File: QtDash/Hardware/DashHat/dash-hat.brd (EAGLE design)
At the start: 120.9 x 74.9 mm, 179 parts, among them IC1 LMV614, IC10 MAX9924, IC11 ZXTR2105FQ, IC12 SN65HVD230D, IC13 MCP2515, IC2 MCP3X083008, IC3 MCP23017SS, IC4 LM358D, IC5 IL300, IC6 TSV912D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

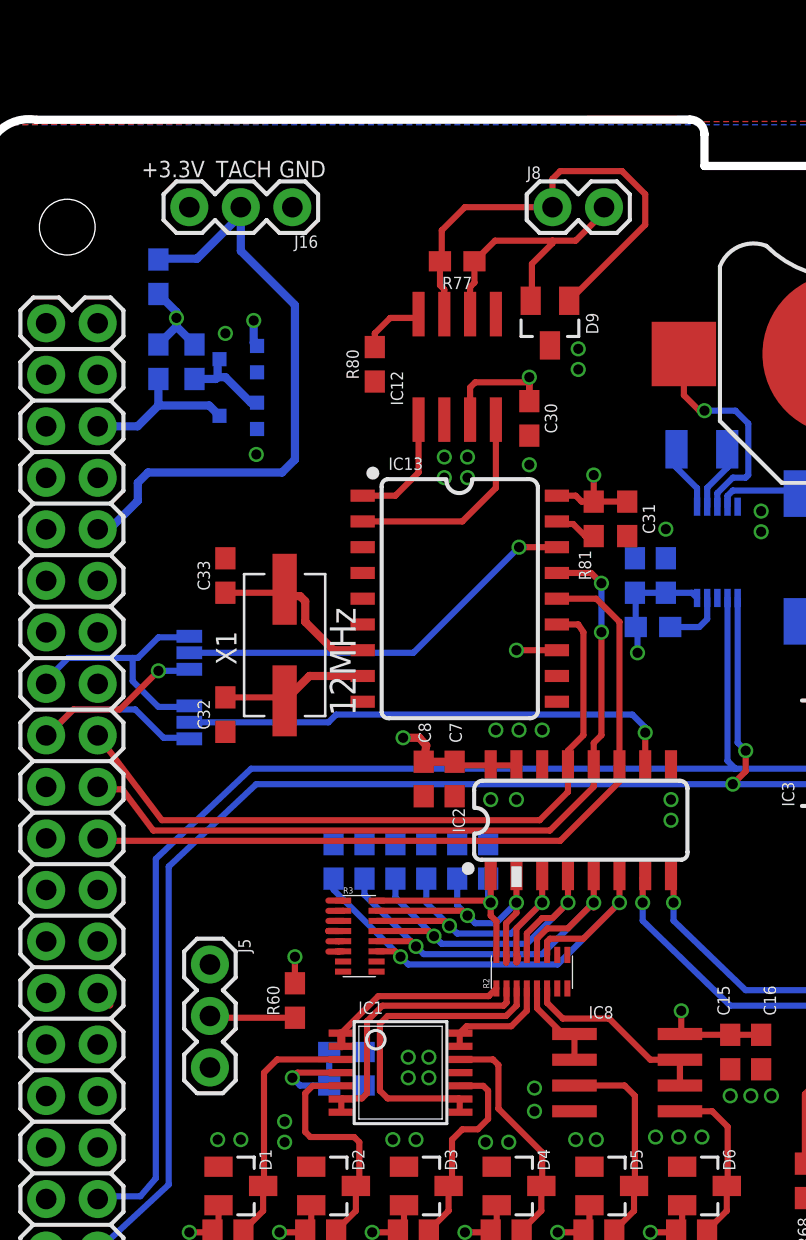
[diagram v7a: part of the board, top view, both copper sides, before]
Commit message: topic/hardware-revc: 	- gerbers generated for rev c 	- pcb's ordered from JLC pcb 	- rev c board preview images generated
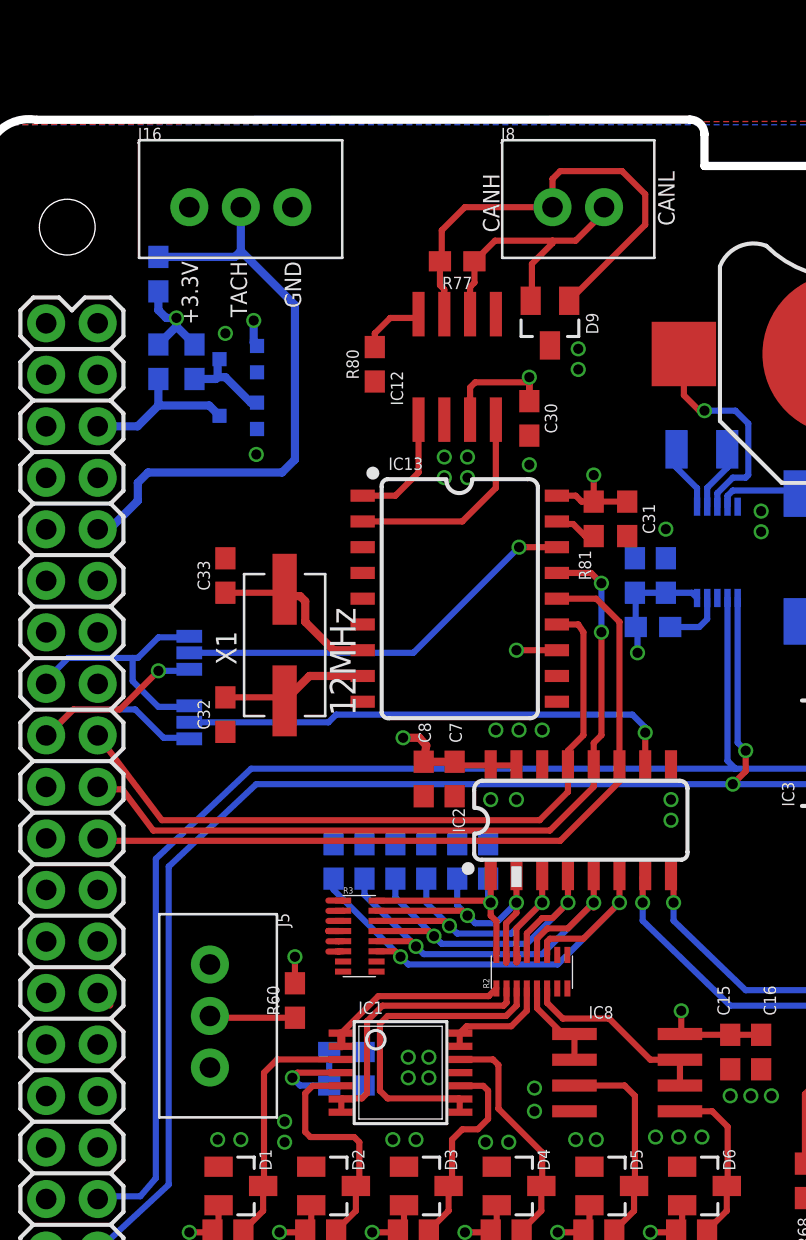
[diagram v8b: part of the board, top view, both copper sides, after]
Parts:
- J16, J5: device SparkFun-Connectors:1X03 -> digital_dash:1X03_JST-XHP
- J8: device digital_dash:1X02 -> digital_dash:1X02_JST-XHP
- moved J16 5.08 mm to (10.2, 62.5), turned to 0 degrees
- moved R76 0.13 mm to (8.64, 59.2)
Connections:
- net 3.3V: now also J16.1; no longer J16.3
- net GND: now also J16.3; no longer J16.1
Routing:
- net GPIO6: track 30.6 -> 29.8 mm
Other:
- board text added: "CANH"
- board text added: "CANL"
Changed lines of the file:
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@@
 Rev C. May 2022
 @whitfijs</text>
-<text x="10.922" y="64.77" size="0.8128" layer="21" font="vector" rot="R180">+3.3V</text>
-<text x="16.891" y="64.77" size="0.8128" layer="21" font="vector" rot="R180">GND</text>
-<text x="14.224" y="64.77" size="0.8128" layer="21" font="vector" rot="R180">TACH</text>
+<text x="9.779" y="59.817" size="0.8128" layer="21" font="vector" rot="R270">+3.3V</text>
+<text x="14.859" y="59.817" size="0.8128" layer="21" font="vector" rot="R270">GND</text>
+<text x="12.192" y="59.817" size="0.8128" layer="21" font="vector" rot="R270">TACH</text>
 <circle x="4.7878" y="18.439" radius="1" width="0.001" layer="57"/>
 <circle x="4.6578" y="27.779" radius="1" width="0.001" layer="57"/>
@@
 <text x="72.39" y="61.595" size="1.016" layer="25" font="vector">12V Switched</text>
 <text x="72.39" y="64.135" size="1.016" layer="25" font="vector">GND</text>
+<text x="33.274" y="64.262" size="0.8128" layer="21" font="vector" rot="R270">CANL</text>
+<text x="24.638" y="64.135" size="0.8128" layer="21" font="vector" rot="R270">CANH</text>
 </plain>
 <attributes>
@@
 <attribute name="SF_SKU" value="COM-08229" x="40.259" y="45.212" size="1.778" layer="28" rot="MR90" display="off"/>
 </element>
-<element name="J16" library="SparkFun-Connectors" package="1X03" value="TACH_IN" x="15.24" y="62.484" rot="R180">
-<attribute name="PROD_ID" value="XXX-00000" x="15.24" y="62.484" size="1.778" layer="27" rot="R180" display="off"/>
-</element>
-<element name="R76" library="digital_dash" package="0603" value="20k" x="8.636" y="59.055" rot="MR270"/>
+<element name="J16" library="digital_dash" package="1X03_JST-XHP" value="TACH_IN" x="10.16" y="62.484"/>
+<element name="R76" library="digital_dash" package="0603" value="20k" x="8.636" y="59.182" rot="MR270"/>
 <element name="R82" library="digital_dash" package="0617/17" value="RES_D+" x="109.474" y="47.879" smashed="yes" rot="R90">
 <attribute name="NAME" x="112.9284" y="56.261" size="1.27" layer="25" font="vector" ratio="10" rot="R270"/>
@@
 <element name="J3" library="digital_dash" package="MOLEX-1053141204" value="CONN_04RIGHT-ANGLE" x="69.469" y="63.373"/>
 <element name="J4" library="digital_dash" package="MOLEX-1053101104" value="CONN_04" x="43.688" y="19.431" rot="R180"/>
-<element name="J5" library="SparkFun-Connectors" package="1X03" value="PWM_OUT" x="11.176" y="25.146" rot="R270">
-<attribute name="PROD_ID" value="XXX-00000" x="11.176" y="25.146" size="1.778" layer="27" rot="R270" display="off"/>
-</element>
+<element name="J5" library="digital_dash" package="1X03_JST-XHP" value="PWM_OUT" x="11.176" y="25.146" rot="R270"/>
 <element name="R60" library="digital_dash" package="0603" value="20k" x="15.367" y="23.368" rot="R90"/>
 <element name="R64" library="digital_dash" package="0603" value="1k" x="42.164" y="14.478" smashed="yes" rot="R90">
@@
 <attribute name="VOLTAGE" value="50V" x="11.938" y="44.323" size="1.778" layer="27" rot="R90" display="off"/>
 </element>
-<element name="J8" library="digital_dash" package="1X02" value="" x="28.067" y="62.484"/>
+<element name="J8" library="digital_dash" package="1X02_JST-XHP" value="" x="28.067" y="62.484"/>
 </elements>
 <signals>
@@
 <contactref element="C14" pad="2"/>
 <contactref element="C11" pad="2"/>
-<contactref element="J16" pad="1"/>
 <via x="33.909" y="33.274" extent="1-16" drill="0.5"/>
 <via x="33.909" y="32.258" extent="1-16" drill="0.5"/>
@@
 <via x="26.924" y="49.784" extent="1-16" drill="0.5"/>
 <via x="33.655" y="46.609" extent="1-16" drill="0.5"/>
+<contactref element="J16" pad="3"/>
 </signal>
 <signal name="5V">
@@
 <wire x1="21.844" y1="35.941" x2="21.502" y2="36.322" width="0.4064" layer="1"/>
 <wire x1="21.502" y1="36.322" x2="20.701" y2="36.322" width="0.4064" layer="1"/>
-<contactref element="J16" pad="3"/>
 <contactref element="R76" pad="2"/>
 <contactref element="R54" pad="2"/>
@@
 <wire x1="10.414" y1="55.714" x2="9.525" y2="56.603" width="0.4064" layer="16"/>
 <wire x1="9.525" y1="56.603" x2="9.525" y2="57.023" width="0.4064" layer="16"/>
-<wire x1="8.636" y1="58.205" x2="9.525" y2="57.316" width="0.4064" layer="16"/>
-<wire x1="9.525" y1="57.316" x2="9.525" y2="57.023" width="0.4064" layer="16"/>
 <wire x1="35.195" y1="43.216" x2="34.938" y2="43.473" width="0.3048" layer="16"/>
 <wire x1="34.938" y1="43.473" x2="33.655" y2="43.473" width="0.3048" layer="16"/>
@@
 <wire x1="26.836" y1="53.848" x2="26.924" y2="53.76" width="0.3048" layer="1"/>
 <wire x1="26.924" y1="53.76" x2="26.924" y2="52.92" width="0.3048" layer="1"/>
+<wire x1="8.636" y1="58.332" x2="8.636" y2="57.404" width="0.4064" layer="16"/>
+<wire x1="8.636" y1="57.404" x2="9.017" y2="57.023" width="0.4064" layer="16"/>
+<wire x1="9.017" y1="57.023" x2="9.525" y2="57.023" width="0.4064" layer="16"/>
+<contactref element="J16" pad="1"/>
 </signal>
 <signal name="!SPI_CS">
@@
 <signal name="GPIO6">
 <contactref element="J1" pad="31"/>
-<contactref element="J16" pad="2"/>
 <contactref element="R76" pad="1"/>
 <wire x1="5.642" y1="46.6" x2="5.651" y2="46.609" width="0.4064" layer="1"/>
-<wire x1="8.636" y1="59.905" x2="8.675" y2="59.944" width="0.4064" layer="16"/>
-<wire x1="8.675" y1="59.944" x2="10.541" y2="59.944" width="0.4064" layer="16"/>
-<wire x1="10.541" y1="59.944" x2="12.7" y2="62.103" width="0.4064" layer="16"/>
-<wire x1="12.7" y1="62.103" x2="12.7" y2="62.484" width="0.4064" layer="16"/>
 <wire x1="15.367" y1="57.658" x2="12.7" y2="60.325" width="0.4064" layer="16"/>
-<wire x1="12.7" y1="60.325" x2="12.7" y2="62.484" width="0.4064" layer="16"/>
 <wire x1="15.367" y1="57.658" x2="15.367" y2="50.038" width="0.4064" layer="16"/>
 <wire x1="15.367" y1="50.038" x2="14.732" y2="49.403" width="0.4064" layer="16"/>
@@
 <wire x1="7.62" y1="48.006" x2="6.214" y2="46.6" width="0.4064" layer="16"/>
 <wire x1="6.214" y1="46.6" x2="5.642" y2="46.6" width="0.4064" layer="16"/>
+<contactref element="J16" pad="2"/>
+<wire x1="12.7" y1="62.103" x2="12.7" y2="62.484" width="0.4064" layer="16"/>
+<wire x1="12.7" y1="60.325" x2="12.7" y2="62.484" width="0.4064" layer="16"/>
+<wire x1="12.7" y1="60.325" x2="12.407" y2="60.032" width="0.4064" layer="16"/>
+<wire x1="12.407" y1="60.032" x2="8.636" y2="60.032" width="0.4064" layer="16"/>
 </signal>
 <signal name="N$42">
